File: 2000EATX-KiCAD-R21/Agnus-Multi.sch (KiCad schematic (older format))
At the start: 18 parts, among them J102 Short for 8327A NTSC or 8375, U101 Agnus_MULTI

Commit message: Add files via upload
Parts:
- JA8: footprint Jumper:SolderJumper-3_P1.3mm_Bridged12_RoundedPad1.0x1.5mm -> Jumper:SolderJumper-3_P1.3mm_Open_RoundedPad1.0x1.5mm; symbol Jumper:SolderJumper_3_Bridged12 -> Jumper:SolderJumper_3_Open
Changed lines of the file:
@@
 Agnus 8375 and 8372A\nMultiadapter
 $Comp
-L Jumper:SolderJumper_3_Bridged12 JA8
+L Jumper:SolderJumper_3_Open JA8
 U 1 1 612754BB
 P 13750 4450
 F 0 "JA8" V 13796 4518 50  0000 L CNN
 F 1 "8375/8372A" V 13705 4518 50  0000 L CNN
-F 2 "Jumper:SolderJumper-3_P1.3mm_Bridged12_RoundedPad1.0x1.5mm" H 13750 4450 50  0001 C CNN
+F 2 "Jumper:SolderJumper-3_P1.3mm_Open_RoundedPad1.0x1.5mm" H 13750 4450 50  0001 C CNN
 F 3 "~" H 13750 4450 50  0001 C CNN
 	1    13750 4450

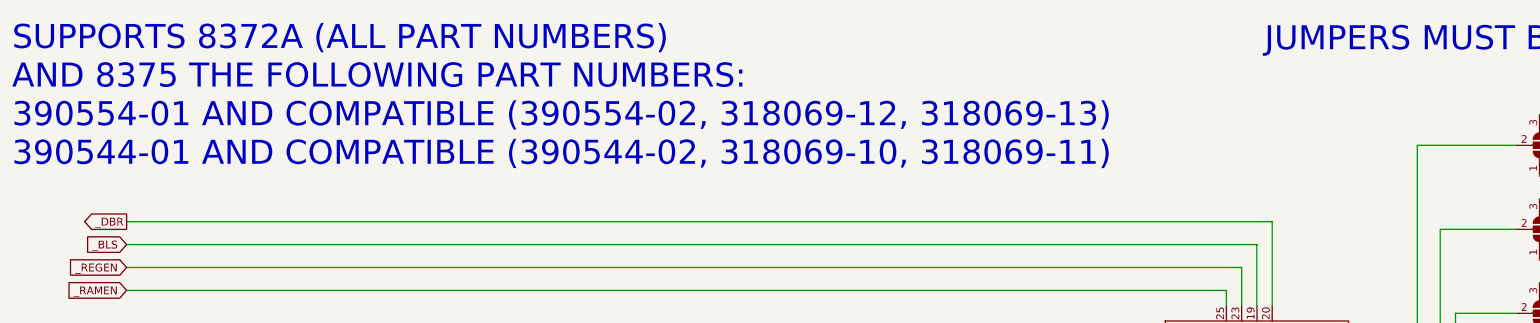
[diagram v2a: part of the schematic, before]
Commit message: Update Rev 2.1 KiCad Agnus Configuration Jumpers
Update the agnus configuration jumper tables in the schematics and on the board.
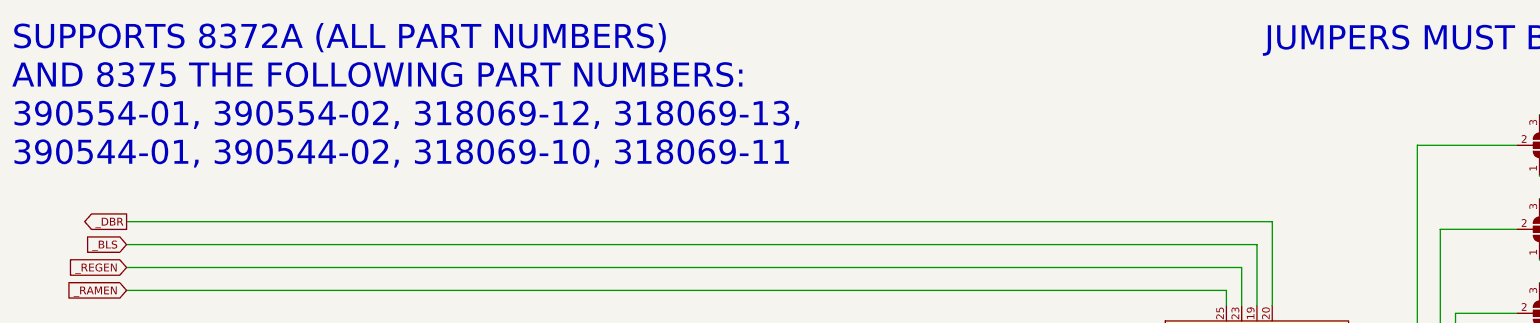
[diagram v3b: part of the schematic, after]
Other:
- note added: "SUPPORTS 8372A (ALL PART NUMBERS)\nAND 8375 THE FOLLOWING PART NUMBERS:\n390554-01, 390554-02, 318069-12, 318069-13,\n390544-01, 390544-02, 318069-10, 318069-11"
- note removed: "SUPPORTS 8372A (ALL PART NUMBERS)\nAND 8375 THE FOLLOWING PART NUMBERS:\n390554-01 AND COMPATIBLE (390554-02, 318069-12, 318069-13)\n390544-01 AND COMPATIBLE (390544-02, 318069-10, 318069-11)"
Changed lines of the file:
@@
 390554-01 is 14M...leave open\n318069-10 is Vbb...short to GND
 Text Notes 800  1600 0    157  ~ 0
-SUPPORTS 8372A (ALL PART NUMBERS)\nAND 8375 THE FOLLOWING PART NUMBERS:\n390554-01 AND COMPATIBLE (390554-02, 318069-12, 318069-13)\n390544-01 AND COMPATIBLE (390544-02, 318069-10, 318069-11)
+SUPPORTS 8372A (ALL PART NUMBERS)\nAND 8375 THE FOLLOWING PART NUMBERS:\n390554-01, 390554-02, 318069-12, 318069-13,\n390544-01, 390544-02, 318069-10, 318069-11
 Text Notes 9000 850  0    157  ~ 0
 JUMPERS MUST BE CONFIGURED BY AGNUS PART NUMBER
